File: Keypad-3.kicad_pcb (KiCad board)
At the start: 2 copper layers, 45.7 x 73.1 mm, 20 parts, among them SW1 SW_Push, U1 ATmega32U4-A, Y1 16MHz

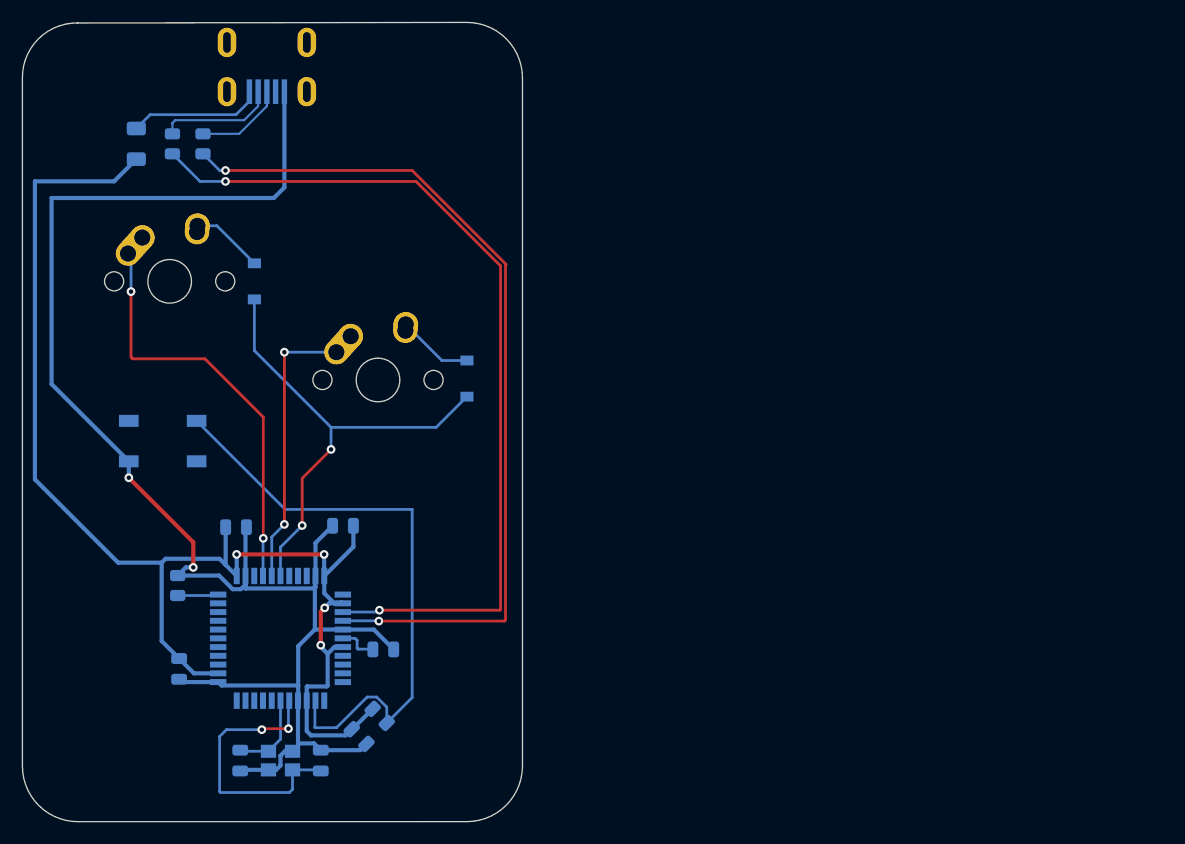
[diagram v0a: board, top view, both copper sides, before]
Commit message: Fixed usb c tracing
I made the usb-c traces straight and re arranged the board to a different layout
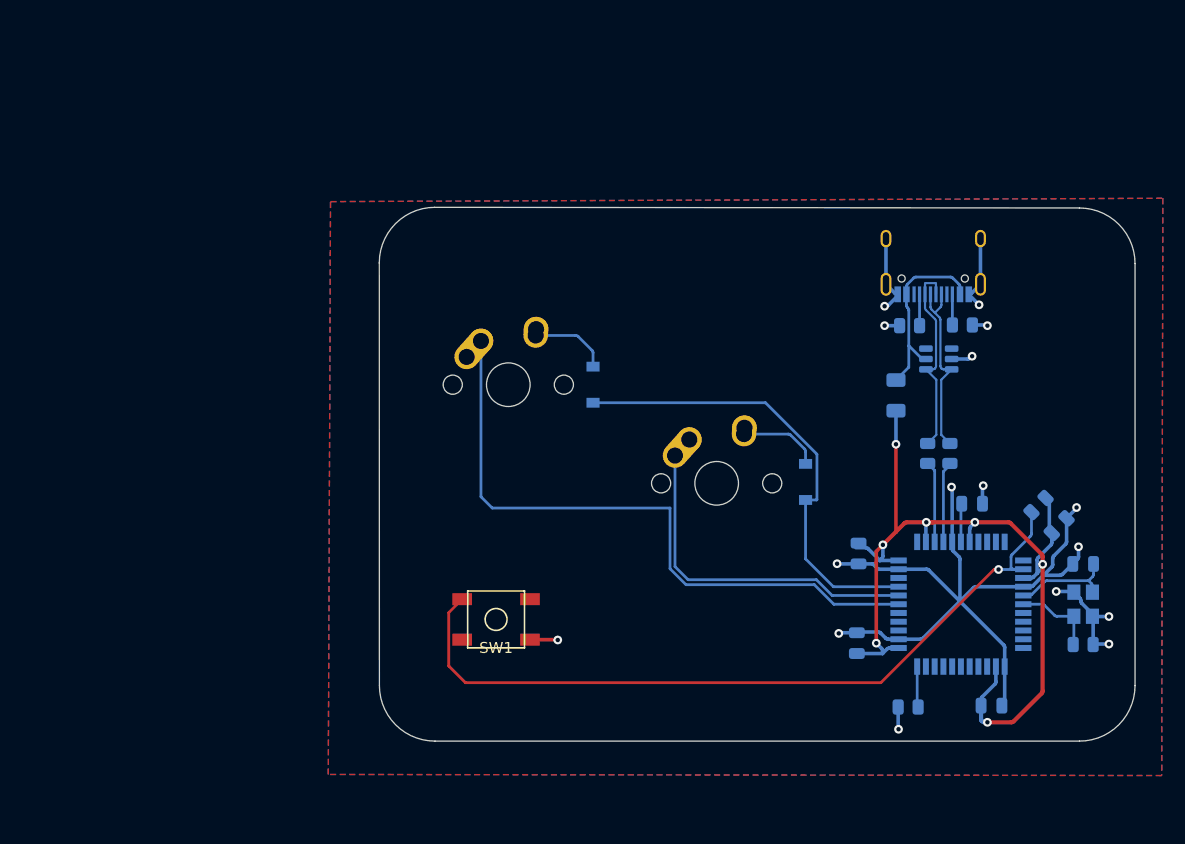
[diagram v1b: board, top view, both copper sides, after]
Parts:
- removed USB1: Molex-0548190589, random-keyboard-parts:Molex-0548190589
- added J1: USB_C_Receptacle_USB2.0, Connector_USB:USB_C_Receptacle_HRO_TYPE-C-31-M-12, B.Cu at (197.4, 99.4)
- added R5: 5.1k, Resistor_SMD:R_0805_2012Metric, B.Cu at (200.1, 106.2)
- added R6: 5.1k, Resistor_SMD:R_0805_2012Metric, B.Cu at (195.3, 106.3)
- added U2: SRV05-4, marbastlib-various:SOT-23-6-routable, B.Cu at (198.0, 109.3)
- C1: footprint Capacitor_SMD:C_0805_2012Metric -> Resistor_SMD:R_0805_2012Metric
- SW1: moved to F.Cu
- moved C1 77.8 mm to (211.2, 135.4), turned to 180 degrees
- moved Y1 74.8 mm to (211.2, 131.8), turned to 90 degrees
- moved R3 74.6 mm to (196.9, 118.0)
- moved C5 74.4 mm to (202.8, 141.0), turned to 0 degrees
- moved R2 73.9 mm to (199.0, 118.0)
- moved F1 73.2 mm to (194.0, 112.7)
- moved C2 72.0 mm to (211.2, 128.1), turned to 0 degrees
- moved R4 67.7 mm to (195.2, 141.2), turned to 0 degrees
- moved C4 66.8 mm to (209.0, 124.6), turned to 45 degrees
- moved R1 63.2 mm to (207.1, 122.7), turned to -135 degrees
- moved U1 62.3 mm to (200.0, 131.8), turned to -90 degrees
- moved C6 57.7 mm to (190.5, 135.3), turned to 90 degrees
- moved C3 55.5 mm to (201.0, 122.6)
- moved C7 47.2 mm to (190.6, 127.1), turned to -90 degrees
- moved SW1 34.6 mm to (157.5, 133.1), turned to 0 degrees
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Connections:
- F1 pad 1: VCC -> VBUS
- U1 pad 37: COL0 -> unconnected-(U1-Pad37)
- U1 pad 38: COL1 -> unconnected-(U1-Pad38)
- U1 pad 39: ROW0 -> COL0
- U1 pad 40: unconnected-(U1-Pad40) -> COL1
- U1 pad 41: unconnected-(U1-Pad41) -> ROW0
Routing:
- net Net-(R3-Pad2): track 80.2 -> 7.46 mm, vias 2 -> 0
- net Net-(R2-Pad2): track 79.4 -> 7.55 mm, vias 2 -> 0
- net GND: track 146.1 -> 106.1 mm, vias 2 -> 16
- net +5V: track 122.5 -> 87.6 mm, vias 4 -> 7
- net COL0: track 38.5 -> 59.7 mm, vias 2 -> 0
- net VBUS: track 0.00 -> 17.6 mm
- net Net-(R1-Pad2): track 55.6 -> 71.5 mm, vias 0 -> 1
- net Net-(C2-Pad2): track 25.4 -> 9.64 mm, vias 2 -> 0
- net VCC: track 12.2 -> 0.00 mm
- net D+: track 8.21 -> 17.6 mm
- net D-: track 10.8 -> 18.5 mm
- net COL1: track 25.7 -> 31.7 mm, vias 2 -> 0
- net Net-(J1-PadA5): track 0.00 -> 2.87 mm
- net Net-(J1-PadB5): track 0.00 -> 2.80 mm
- net ROW0: track 43.7 -> 42.6 mm, vias 2 -> 0
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- added copper zone on B.Cu, net GND
- added copper zone on F.Cu, net GND
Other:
- board size 45.7 x 73.1 mm -> 69.1 x 48.8 mm

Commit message: re-arranged some tracings
Better tracing arrangement
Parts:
- moved R1 1.28 mm to (207.3, 124.0), turned to -90 degrees
- moved C4 0.79 mm to (209.4, 124.0), turned to 90 degrees
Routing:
- net +5V: track 87.6 -> 104.6 mm, vias 7 -> 5
- net GND: track 106.1 -> 92.7 mm, vias 16 -> 17
- net Net-(R1-Pad2): track 71.5 -> 78.7 mm
- net Net-(D2-Pad2): track 7.47 -> 13.7 mm
- net Net-(D1-Pad2): track 7.22 -> 13.2 mm
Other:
- board size 69.1 x 48.8 mm -> 69.1 x 49 mm

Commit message: Made the gerber files
:D
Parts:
- moved F1 2.78 mm to (194.0, 109.9)
- moved J1 2.78 mm to (197.4, 96.6)
- moved R5 2.78 mm to (200.1, 103.4)
- moved R6 2.78 mm to (195.3, 103.5)
- moved U2 2.78 mm to (198.0, 106.6)
- moved C4 0.92 mm to (210.0, 123.2)
- moved R1 0.92 mm to (207.8, 123.2)
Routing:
- net Net-(D2-Pad2): track 13.7 -> 6.76 mm
- net Net-(D1-Pad2): track 13.2 -> 6.52 mm
- net D+: track 17.5 -> 20.3 mm
- net D-: track 18.5 -> 21.3 mm
- net +5V: track 104.6 -> 107.3 mm
- net COL0: track 59.7 -> 57.2 mm
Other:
- board size 69.1 x 49 mm -> 69.1 x 50.3 mm
- board text added: ":P"
- board text added: "By Nickgem25"

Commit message: Final Design (for real this time I think)
Removed the switch.
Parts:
- removed SW1: SW_Push, random-keyboard-parts:SKQG-1155865
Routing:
- net Net-(R1-Pad2): track 78.9 -> 5.84 mm, vias 1 -> 0
- net GND: track 92.7 -> 90.2 mm, vias 17 -> 16
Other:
- board size 69.1 x 50.3 mm -> 68.6 x 50.8 mm
